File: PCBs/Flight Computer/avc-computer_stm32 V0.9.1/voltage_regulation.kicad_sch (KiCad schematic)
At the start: 20 parts, among them IC1 MP2307, U7 LD1117S33TR_SOT223

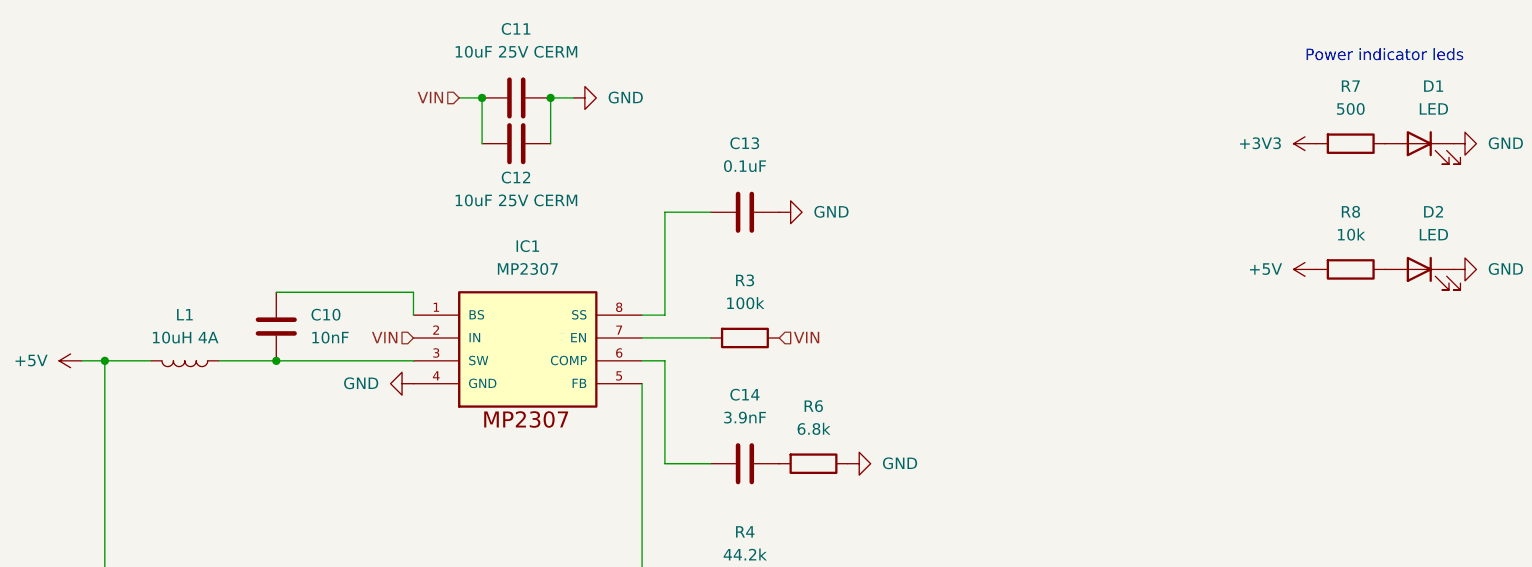
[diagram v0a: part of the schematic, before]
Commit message: Fixed all issues except for 5v buck inductor heating
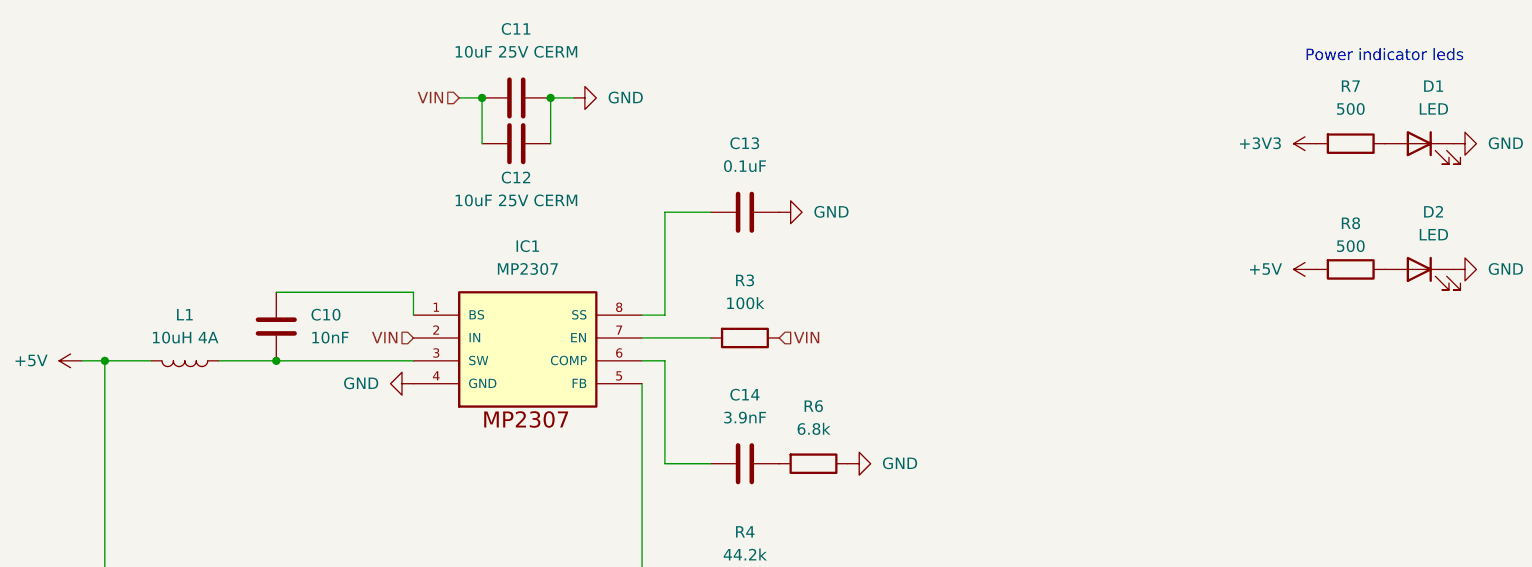
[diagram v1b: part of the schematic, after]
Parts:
- R8: value 10k -> 500
